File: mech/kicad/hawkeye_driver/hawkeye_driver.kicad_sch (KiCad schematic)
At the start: 27 parts, among them J1 Conn_01x03_Male, J2 Screw_Terminal_01x02, Q1 IRLD024, Q2 IRLD024, Q3 IRLD024, U1 74HC595

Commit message: work on ground planes
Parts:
- removed J1: Conn_01x03_Male, Connector_PinHeader_2.54mm:PinHeader_1x03_P2.54mm_Vertical, symbol Connector:Conn_01x03_Male
- removed R20: 2k, Resistor_THT:R_Axial_DIN0207_L6.3mm_D2.5mm_P5.08mm_Vertical, symbol Device:R_US
- removed R21: 5k, Resistor_THT:R_Axial_DIN0207_L6.3mm_D2.5mm_P5.08mm_Vertical, symbol Device:R_US
- added C1: 1 uF, Capacitor_SMD:C_1206_3216Metric_Pad1.33x1.80mm_HandSolder, symbol Device:C
- added J1: Conn_02x05_Odd_Even, Connector_IDC:IDC-Header_2x05_P2.54mm_Vertical, symbol Connector_Generic:Conn_02x05_Odd_Even
- R14, R15, R16, R17, R18, R19: footprint Resistor_THT:R_Axial_DIN0207_L6.3mm_D2.5mm_P5.08mm_Vertical -> Resistor_SMD:R_1206_3216Metric_Pad1.30x1.75mm_HandSolder
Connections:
- net GND: now also C1.2, J1.1 (Pin_1), J1.10 (Pin_10), J1.3 (Pin_3), J1.5 (Pin_5), J1.7 (Pin_7), J1.9 (Pin_9)
- net LATCH: now also J1.8 (Pin_8)
- net SER IN: now also J1.4 (Pin_4)
- net SHIFT CLK: now also J1.6 (Pin_6)
- net INNER_RING_LOW: now reaches Q1.1 (D), R1.1, R2.1, R3.1, R4.1, R5.1, R6.1
- net CENTER_LOW: now reaches Q3.1 (D), R13.1
- net OUTER_RING_LOW: now reaches Q2.1 (D), R10.1, R11.1, R12.1, R7.1, R8.1, R9.1
- net 4.78 V (req. > 4V) renamed 5V
- net 5V: now also C1.1, J1.2 (Pin_2)
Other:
- note removed: "N.B.: Ensure MCU signal GND is common to heater supply GND"

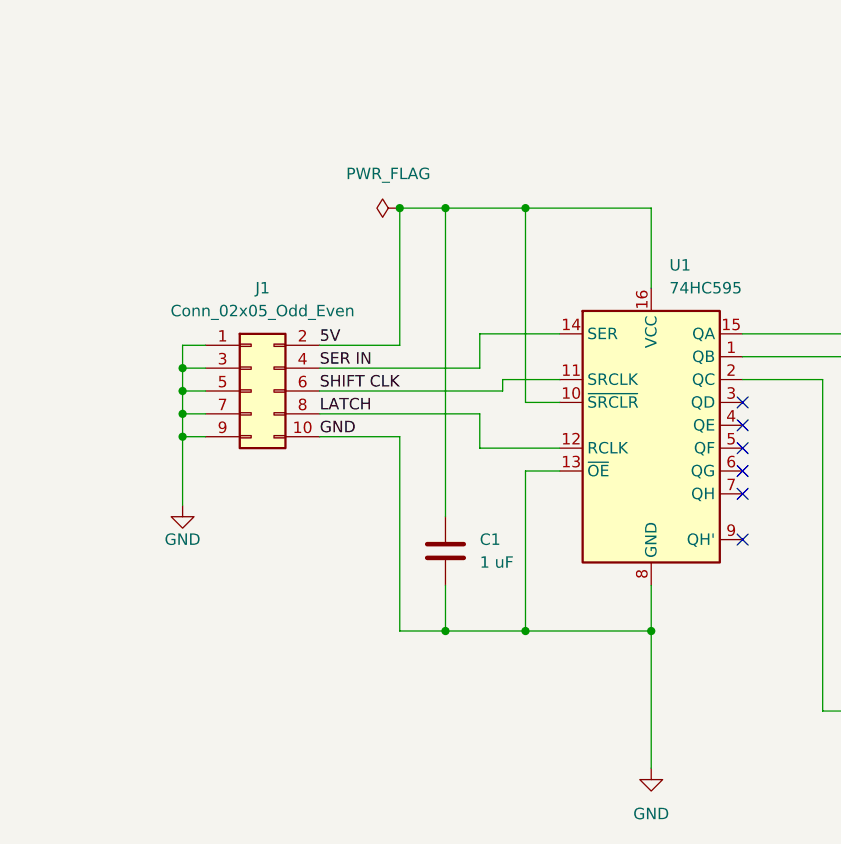
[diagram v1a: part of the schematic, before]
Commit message: finish ground plane rework
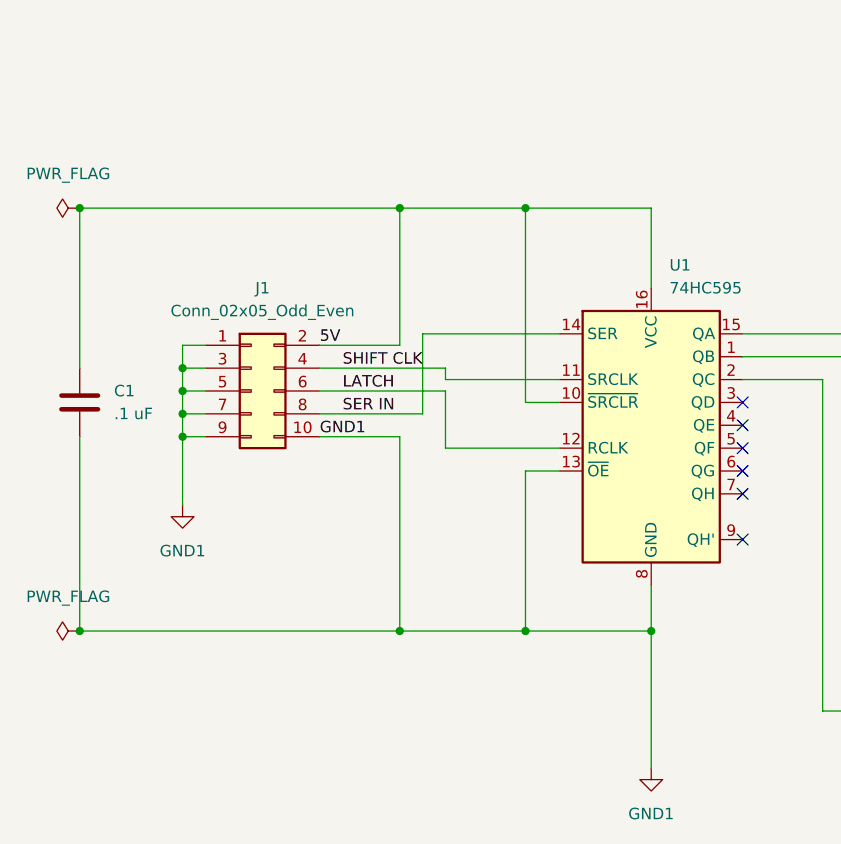
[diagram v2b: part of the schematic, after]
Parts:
- C1: value 1 uF -> .1 uF
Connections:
- net GND: no longer C1.2, J1.1 (Pin_1), J1.10 (Pin_10), J1.3 (Pin_3), J1.5 (Pin_5), J1.7 (Pin_7), J1.9 (Pin_9), U1.13 (~{OE}), U1.8 (GND)
- net LATCH: now also J1.6 (Pin_6); no longer J1.8 (Pin_8)
- net SER IN: now also J1.8 (Pin_8); no longer J1.4 (Pin_4)
- net SHIFT CLK: now also J1.4 (Pin_4); no longer J1.6 (Pin_6)
- new net GND1: C1.2, J1.1 (Pin_1), J1.10 (Pin_10), J1.3 (Pin_3), J1.5 (Pin_5), J1.7 (Pin_7), J1.9 (Pin_9), U1.13 (~{OE}), U1.8 (GND)
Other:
- moved on the sheet: C1

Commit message: final commit before fab
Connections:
- net GND1: no longer J1.10 (Pin_10)
- no-connect marks 6 -> 7
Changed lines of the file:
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@@
   (junction (at 171.45 119.38) (diameter 0) (color 0 0 0 0)
-  )
-  (junction (at 76.2 123.19) (diameter 0) (color 0 0 0 0)
   )
   (junction (at 90.17 76.2) (diameter 0) (color 0 0 0 0)
@@
   (no_connect (at 114.3 105.41))
   (no_connect (at 114.3 107.95))
+  (no_connect (at 67.31 101.6))
   (no_connect (at 114.3 102.87))
   (no_connect (at 114.3 97.79))
@@
     (stroke (width 0) (type default) (color 0 0 0 0))
   )
-  (wire (pts (xy 76.2 123.19) (xy 90.17 123.19))
-    (stroke (width 0) (type default) (color 0 0 0 0))
-  )
   (wire (pts (xy 144.78 62.23) (xy 163.83 62.23))
     (stroke (width 0) (type default) (color 0 0 0 0))
@@
     (stroke (width 0) (type default) (color 0 0 0 0))
   )
-  (wire (pts (xy 67.31 101.6) (xy 76.2 101.6))
-    (stroke (width 0) (type default) (color 0 0 0 0))
-  )
   (wire (pts (xy 81.28 102.87) (xy 93.98 102.87))
     (stroke (width 0) (type default) (color 0 0 0 0))
@@
     (stroke (width 0) (type default) (color 0 0 0 0))
   )
-  (wire (pts (xy 76.2 101.6) (xy 76.2 123.19))
-    (stroke (width 0) (type default) (color 0 0 0 0))
-  )
   (wire (pts (xy 171.45 85.09) (xy 171.45 88.9))
     (stroke (width 0) (type default) (color 0 0 0 0))
@@
     (stroke (width 0) (type default) (color 0 0 0 0))
   )
-  (wire (pts (xy 40.64 123.19) (xy 76.2 123.19))
+  (wire (pts (xy 40.64 123.19) (xy 90.17 123.19))
     (stroke (width 0) (type default) (color 0 0 0 0))
   )
@@
     (effects (font (size 1.27 1.27)) (justify left bottom))
   )
-  (label "GND1" (at 67.31 101.6 0)
-    (effects (font (size 1.27 1.27)) (justify left bottom))
-  )
